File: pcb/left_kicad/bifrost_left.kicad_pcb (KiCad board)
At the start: 2 copper layers, 142.9 x 80.3 mm, 68 parts, among them J1 HRO_TYPE-C-31-M-12, J2 Conn_01x02, J3 Conn_01x06, Q1 AO3401A, Q2 2N7002, Q3 AO3401A, SW1 1.5U, SW10 1U, SW11 1U, SW12 1.25U, SW13 1U, SW14 1U, SW15 1U, SW16 1U, SW17 1U, SW18 1U, SW19 1U, SW2 1.75U, SW20 1U, SW21 1U, SW3 2U, SW4 1.25U, SW5 1U, SW6 1U, SW7 1U, SW8 1.25U, SW9 1U, T1 TS24CA, U1 MDBT50Q-1MV2, U2 TP4057, U3 SRV05-4, X1 32.768kHz

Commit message: Refactor application structure and update implementation
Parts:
- R3: value 1.5k -> 1k
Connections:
- SW11 pad 1: PIN_15 -> PIN_11
- SW15 pad 1: PIN_18 -> PIN_15
- SW18 pad 1: PIN_21 -> PIN_18
- SW21 pad 1: PIN_22 -> PIN_21
- SW7 pad 1: PIN_11 -> PIN_7
- U1 pad 11: PIN_21 -> PIN_18
- U1 pad 23: PIN_22 -> PIN_21
- U1 pad 5: PIN_15 -> PIN_11
- U1 pad 57: PIN_11 -> PIN_7
- U1 pad 9: PIN_18 -> PIN_15
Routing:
- net PIN_7: track 0.00 -> 124.9 mm, vias 0 -> 1
- net PIN_22: track 41.7 -> 0.00 mm, vias 1 -> 0
- net PIN_21: track 64.5 -> 41.7 mm
- net PIN_15: track 105.7 -> 84.7 mm
- net PIN_18: track 84.7 -> 64.5 mm
- net PIN_11: track 124.9 -> 105.7 mm

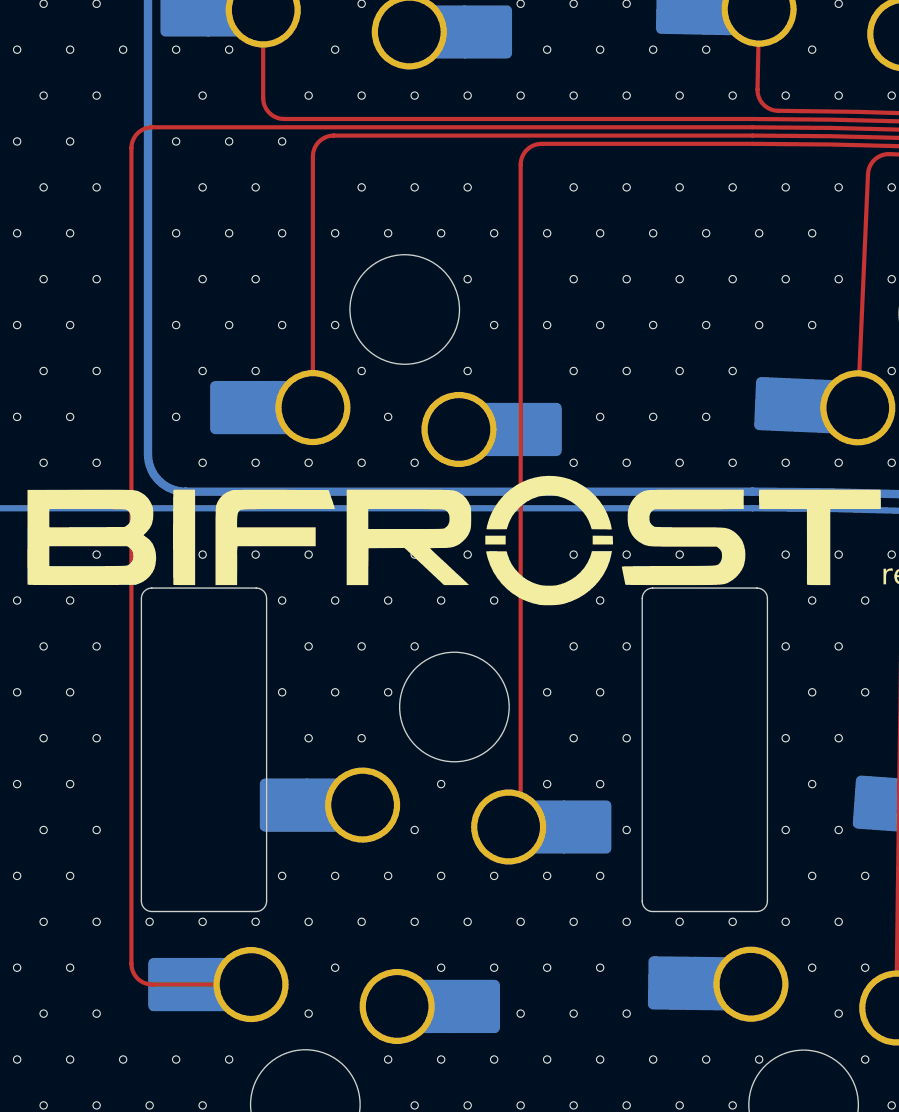
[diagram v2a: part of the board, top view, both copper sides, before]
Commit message: Update PCB plate and stabilizer designs
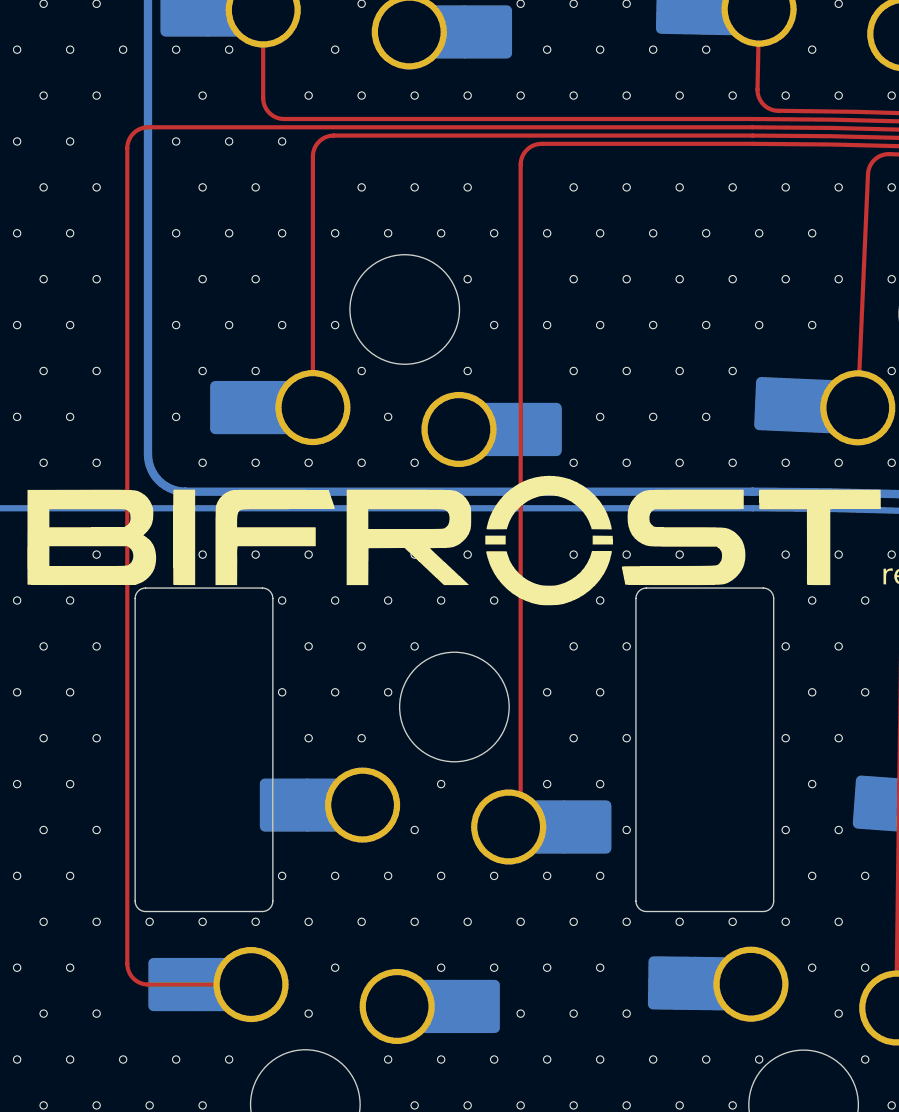
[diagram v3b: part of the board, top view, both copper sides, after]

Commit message: Update PCB circuits and manufacturing data
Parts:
- removed the C8 at (115.5, 53.0)
- removed the D1 at (95.2, 52.5)
- renumbered C9 to C8, D3 to D1, L3 to L2, L2 to L3, Q3 to Q1, Q1 to Q3, R5 to R1, R7 to R10, R8 to R11, R9 to R12, R4 to R13, R6 to R2, R10 to R3, R11 to R4, R12 to R5, R1 to R6, R2 to R7, R13 to R8, R3 to R9, SW14 to SW10, SW17 to SW11, SW20 to SW12, SW3 to SW13, SW7 to SW14, SW11 to SW15, SW15 to SW16, SW18 to SW17, SW21 to SW18, SW4 to SW19, SW5 to SW2, SW8 to SW20, SW12 to SW21, SW9 to SW3, SW13 to SW4, SW16 to SW5, SW19 to SW6, SW2 to SW7, SW6 to SW8, SW10 to SW9, U3 to U1, U1 to U2, U2 to U3
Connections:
- J1 pad A1: Earth -> GND
- J1 pad A12: Earth -> GND
- J1 pad B1: Earth -> GND
- J1 pad B12: Earth -> GND
- J1 pad SH: Earth -> Net-(J1-SHIELD)
- L3 pad 1: Earth -> Net-(J1-SHIELD)
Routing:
- net Earth: track 14.1 -> 0.00 mm
- net Net-(J1-SHIELD): track 0.00 -> 3.32 mm
- net GND: vias 959 -> 963
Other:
- board text added: "rev.0.2"
- board text removed: "rev.0.1"
